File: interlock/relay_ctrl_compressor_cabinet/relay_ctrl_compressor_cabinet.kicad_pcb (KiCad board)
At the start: 2 copper layers, 81.9 x 52.1 mm, 19 parts, among them J1 DB15_Male_MountingHoles, J2 DB15_Male_MountingHoles, J3 RJ45_Shielded, J4 Conn_01x03, J5 Conn_01x02, J6 Conn_01x04, J7 Conn_01x04, U1 LM7805_TO220, U2 4504, U3 TLP222A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

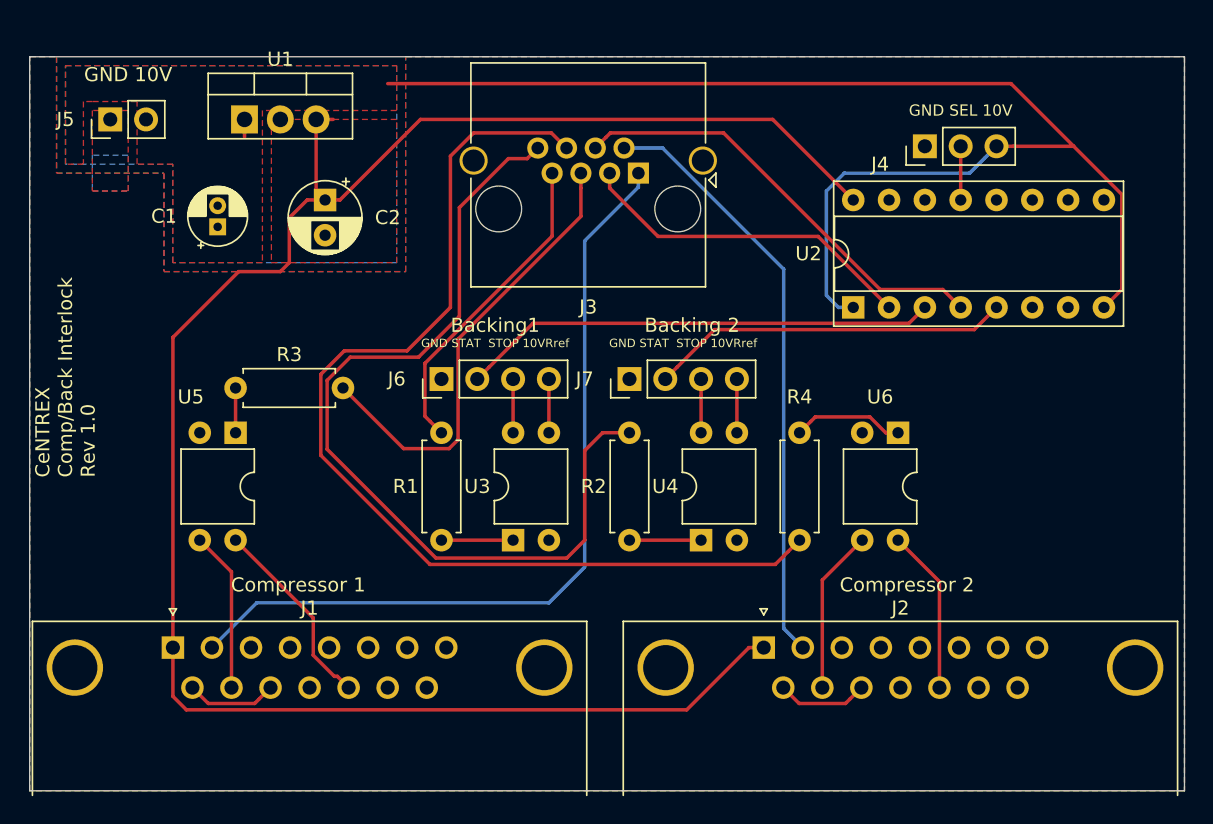
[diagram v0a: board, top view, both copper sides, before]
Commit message: Fixed mistakes in interlock pcbs
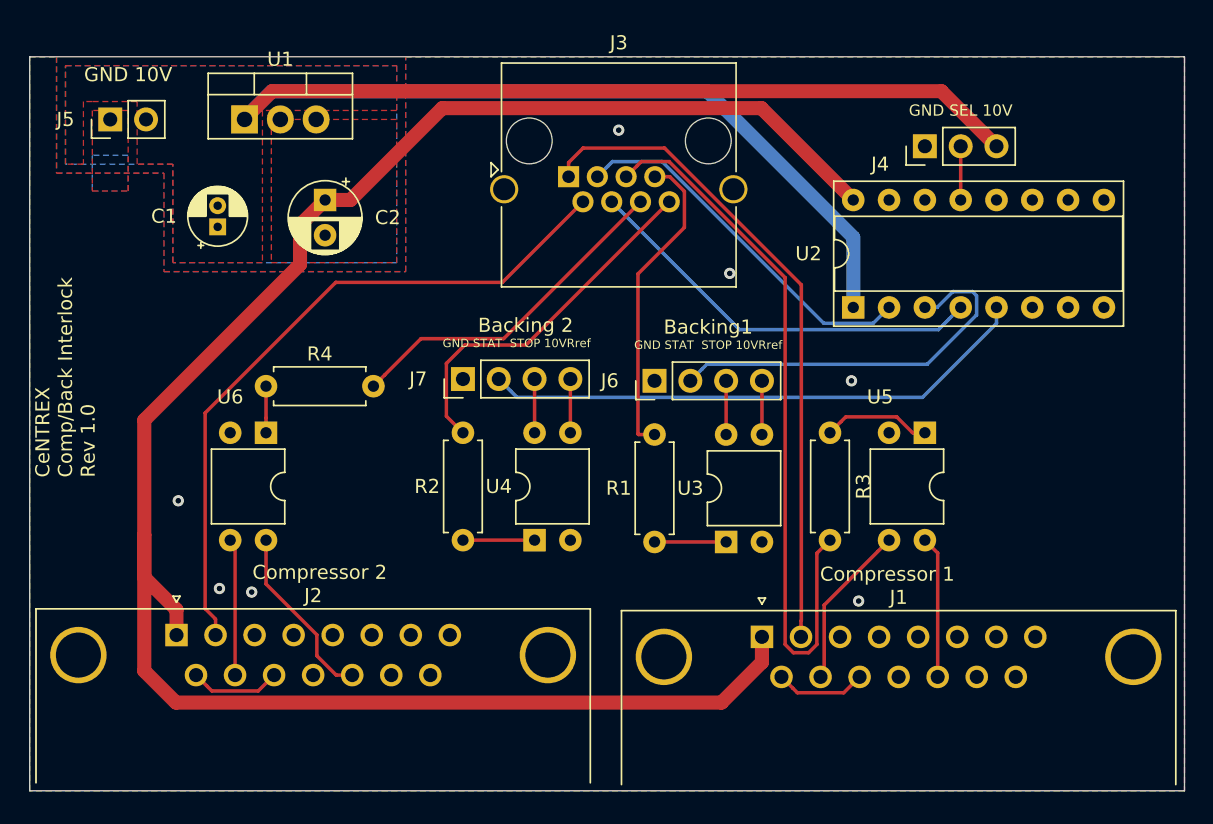
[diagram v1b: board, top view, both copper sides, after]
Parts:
- moved U5 48.9 mm to (144.1, 108.6)
- moved U6 44.8 mm to (97.4, 108.6)
- moved R3 42.3 mm to (137.4, 108.6), turned to 270 degrees
- moved J1 41.8 mm to (132.6, 123.1)
- moved J2 41.7 mm to (91.1, 122.9)
- moved R4 38.0 mm to (97.4, 105.3), turned to 0 degrees
- moved J6 15.1 mm to (125.0, 104.9)
- moved R1 15.1 mm to (125.0, 116.3)
- moved U3 15.1 mm to (130.0, 116.3)
- moved U4 11.8 mm to (116.5, 116.2)
- moved J7 11.8 mm to (111.4, 104.8)
- moved R2 11.8 mm to (111.4, 116.2)
- moved J3 4.96 mm to (118.9, 90.4), turned to 0 degrees
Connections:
- U2 pad 8: +10V -> GND
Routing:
- net Compressor2_interlock: track 74.9 -> 24.4 mm
- net Backing2_interlock: track 63.2 -> 26.0 mm
- net Compressor1_interlock: track 32.7 -> 51.7 mm
- net +10V: track 93.6 -> 109.1 mm
- net Backing2_status: track 25.6 -> 39.2 mm
- net Compressor1_active: track 58.3 -> 46.9 mm
- net Compressor2_active: track 42.3 -> 49.1 mm
- net Backing1_status: track 33.9 -> 27.9 mm
- net Net-(R4-Pad1): track 7.92 -> 3.30 mm
- net Net-(R3-Pad1): track 3.17 -> 7.66 mm
- net /Compressor1_remoteinterlock: track 13.9 -> 10.1 mm
- net Backing2_active: track 31.5 -> 29.2 mm
- net Backing1_active: track 24.4 -> 26.4 mm
- net /Compressor2_24Vreturn: track 11.6 -> 9.71 mm
- net +5V: track 135.7 -> 137.4 mm
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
